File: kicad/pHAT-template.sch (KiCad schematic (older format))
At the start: 1 part

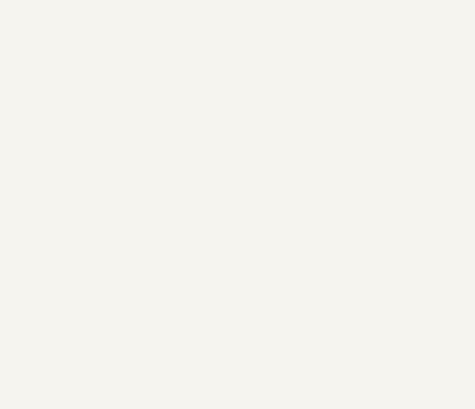
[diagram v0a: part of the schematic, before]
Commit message: added mounting holes and footprints
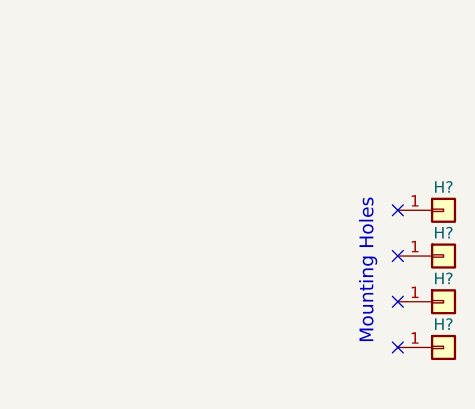
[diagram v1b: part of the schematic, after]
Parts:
- added H? (x4): Conn_01x01, Mounting_Holes:MountingHole_2.7mm_M2.5, symbol Conn_01x01
- J?: footprint (none) -> Pin_Headers:Pin_Header_Straight_2x20_Pitch2.54mm
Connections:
- no-connect marks 0 -> 4
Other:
- note added: "Mounting Holes"
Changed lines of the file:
@@
 F 0 "J?" H 2350 3100 50  0000 C CNN
 F 1 "Conn_02x20_Odd_Even" H 2350 1000 50  0001 C CNN
-F 2 "" H 2300 2100 50  0001 C CNN
+F 2 "Pin_Headers:Pin_Header_Straight_2x20_Pitch2.54mm" H 2300 2100 50  0001 C CNN
 F 3 "" H 2300 2100 50  0001 C CNN
 	1    2300 2100
@@
 Text Label 2100 3000 2    60   ~ 0
 BCM26
+$Comp
+L Conn_01x01 H?
+U 1 1 5A524F17
+P 6650 6900
+F 0 "H?" H 6650 7000 50  0000 C CNN
+F 1 "Conn_01x01" H 6650 6800 50  0001 C CNN
+F 2 "Mounting_Holes:MountingHole_2.7mm_M2.5" H 6650 6900 50  0001 C CNN
+F 3 "" H 6650 6900 50  0001 C CNN
+	1    6650 6900
+	1    0    0    -1
+$EndComp
+$Comp
+L Conn_01x01 H?
+U 1 1 5A525008
+P 6650 7100
+F 0 "H?" H 6650 7200 50  0000 C CNN
+F 1 "Conn_01x01" H 6650 7000 50  0001 C CNN
+F 2 "Mounting_Holes:MountingHole_2.7mm_M2.5" H 6650 7100 50  0001 C CNN
+F 3 "" H 6650 7100 50  0001 C CNN
+	1    6650 7100
+	1    0    0    -1
+$EndComp
+$Comp
+L Conn_01x01 H?
+U 1 1 5A525029
+P 6650 7300
+F 0 "H?" H 6650 7400 50  0000 C CNN
+F 1 "Conn_01x01" H 6650 7200 50  0001 C CNN
+F 2 "Mounting_Holes:MountingHole_2.7mm_M2.5" H 6650 7300 50  0001 C CNN
+F 3 "" H 6650 7300 50  0001 C CNN
+	1    6650 7300
+	1    0    0    -1
+$EndComp
+$Comp
+L Conn_01x01 H?
+U 1 1 5A525049
+P 6650 7500
+F 0 "H?" H 6650 7600 50  0000 C CNN
+F 1 "Conn_01x01" H 6650 7400 50  0001 C CNN
+F 2 "Mounting_Holes:MountingHole_2.7mm_M2.5" H 6650 7500 50  0001 C CNN
+F 3 "" H 6650 7500 50  0001 C CNN
+	1    6650 7500
+	1    0    0    -1
+$EndComp
+NoConn ~ 6450 6900
+NoConn ~ 6450 7100
+NoConn ~ 6450 7300
+NoConn ~ 6450 7500
+Text Notes 6350 6850 3    60   ~ 0
+Mounting Holes
 $EndSCHEMATC

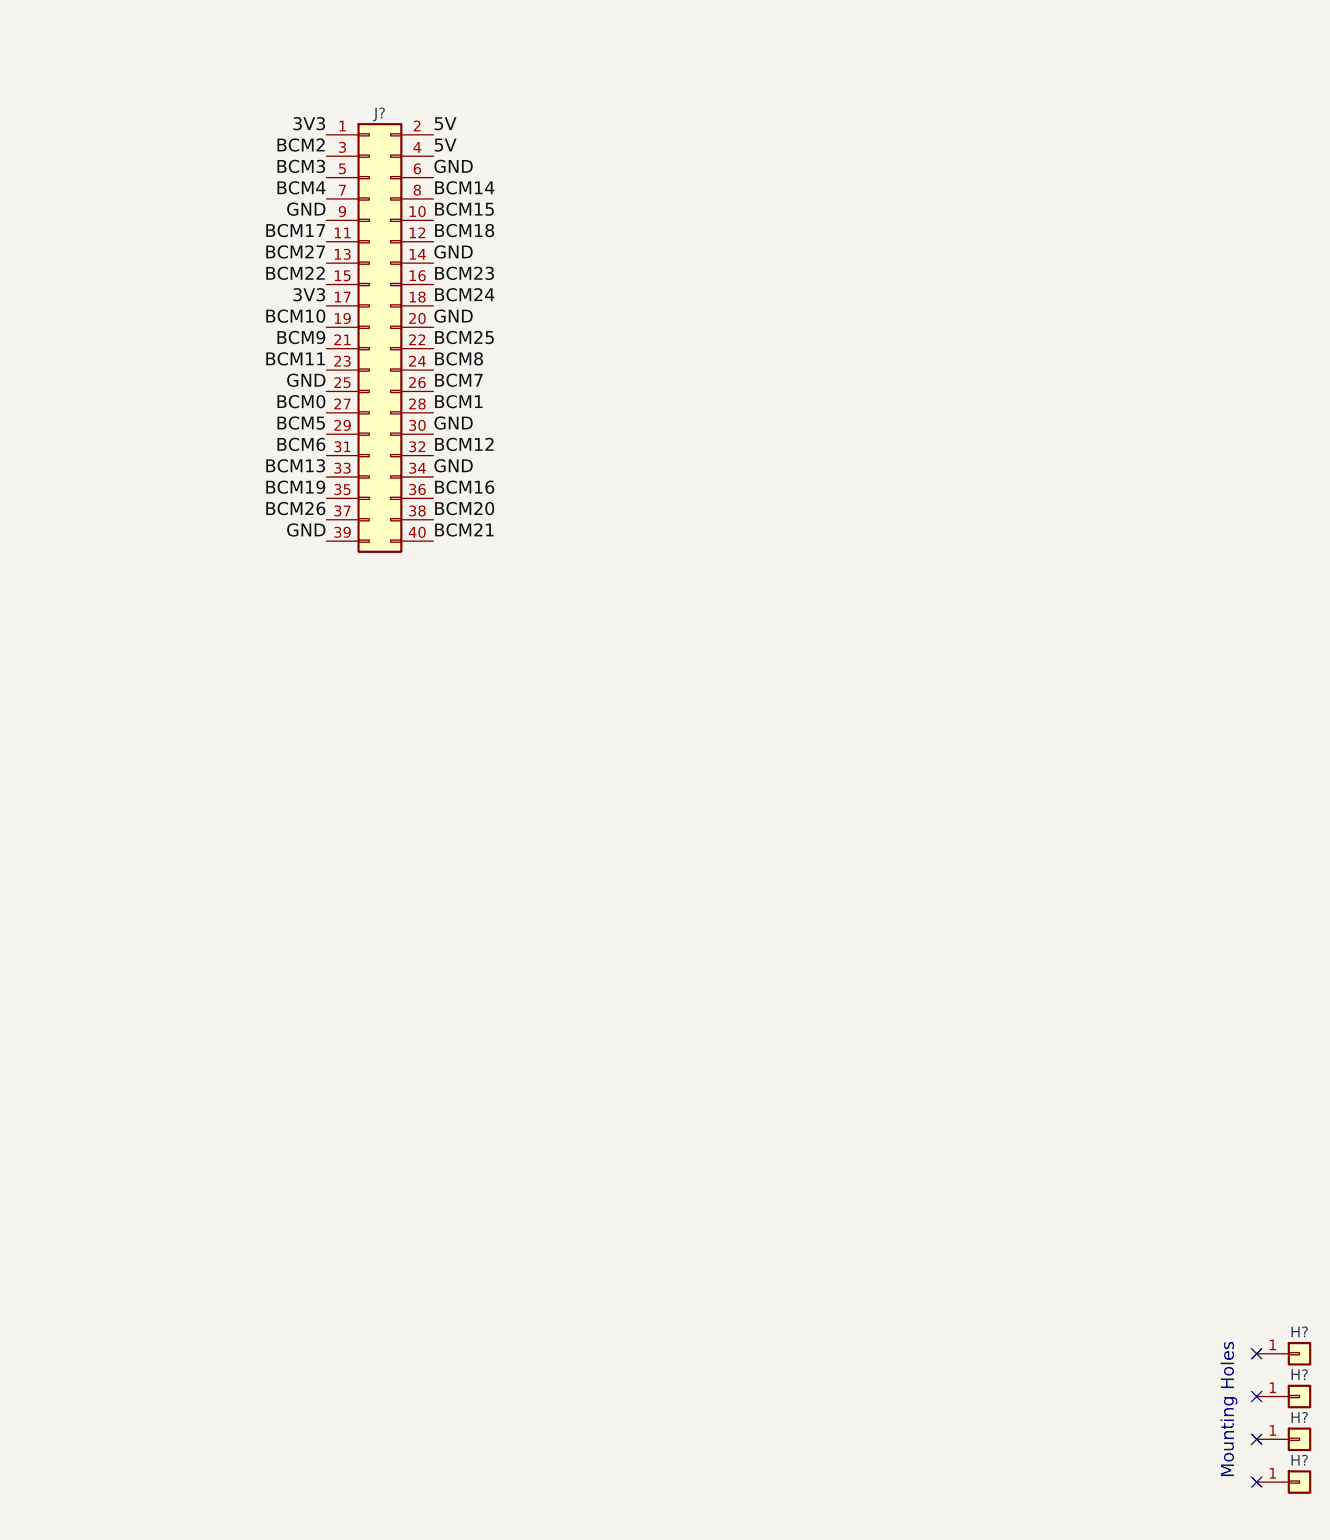
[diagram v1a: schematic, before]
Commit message: annotate schematic, generate netlist
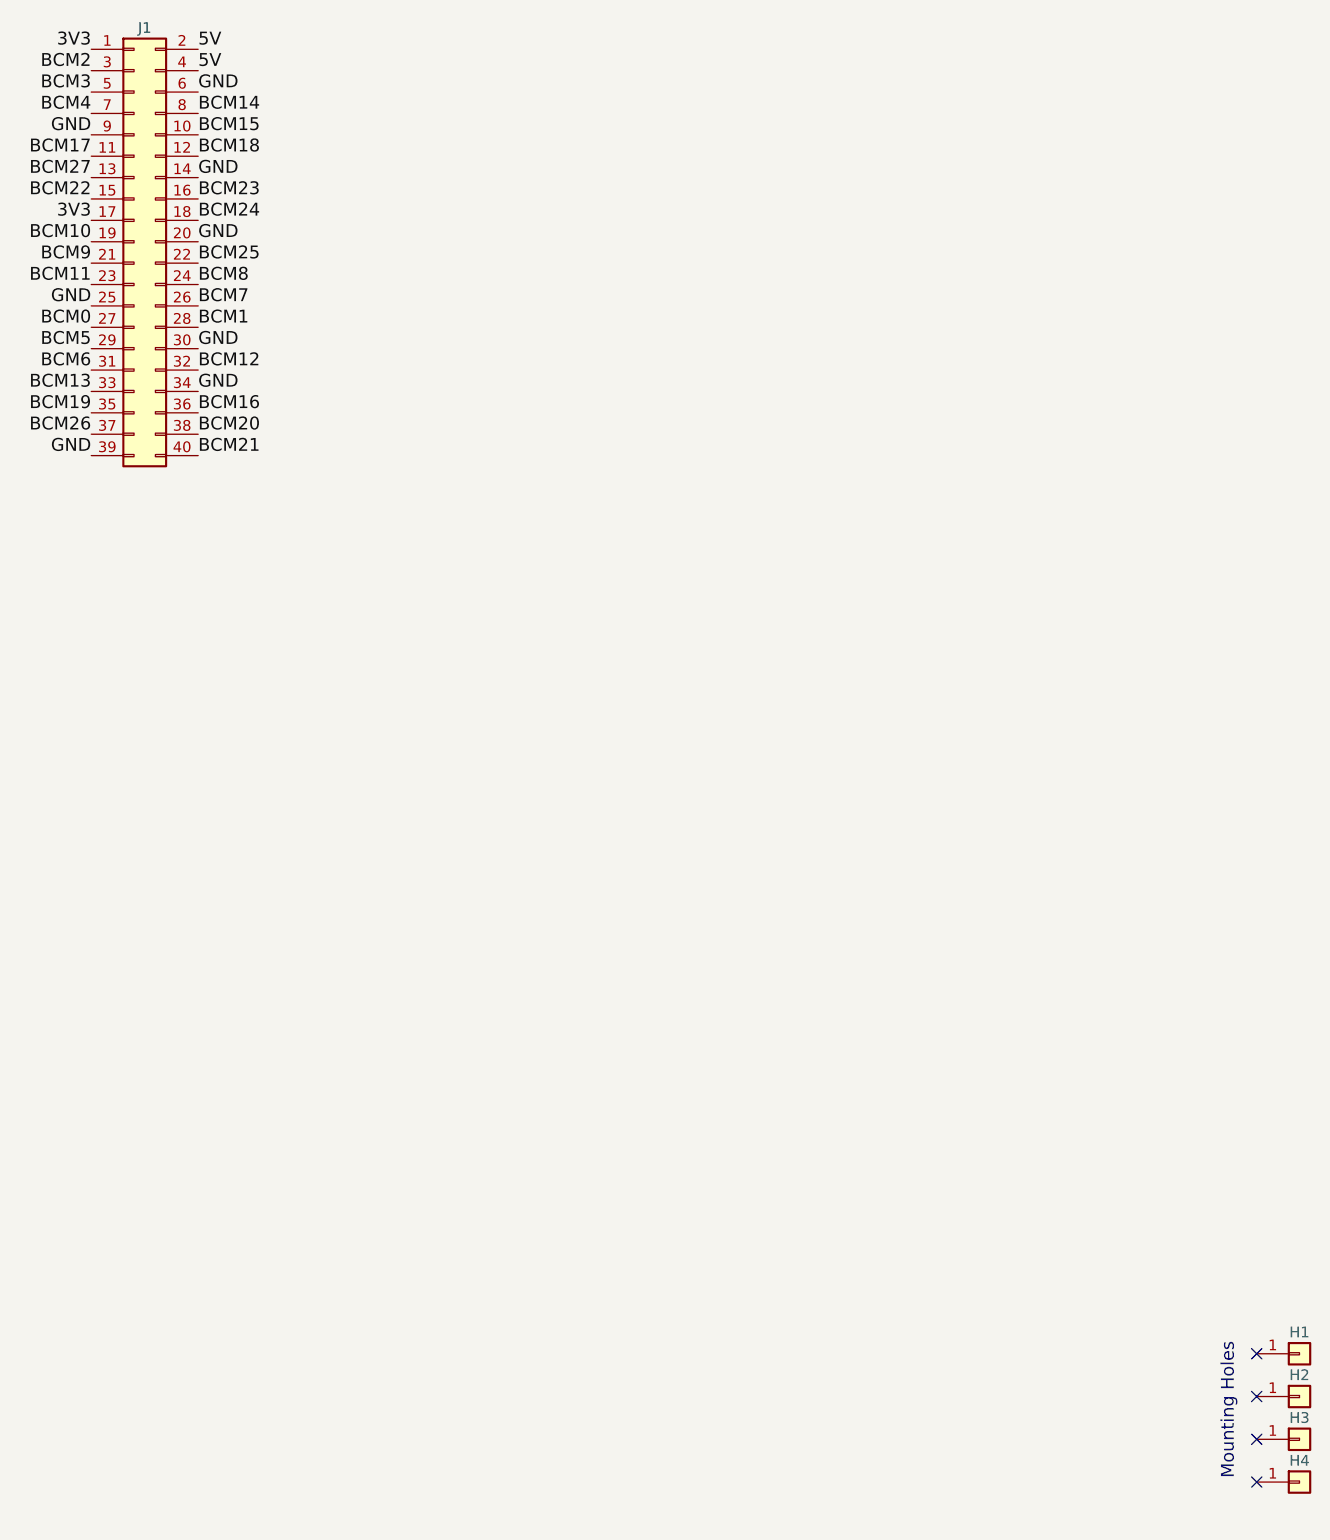
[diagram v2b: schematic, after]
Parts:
- gave numbers to parts that had none: 5
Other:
- moved on the sheet: J1
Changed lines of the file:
@@
 $EndDescr
 $Comp
-L Conn_02x20_Odd_Even J?
+L Conn_02x20_Odd_Even J1
 U 1 1 5A524BD5
-P 2300 2100
-F 0 "J?" H 2350 3100 50  0000 C CNN
-F 1 "Conn_02x20_Odd_Even" H 2350 1000 50  0001 C CNN
-F 2 "Pin_Headers:Pin_Header_Straight_2x20_Pitch2.54mm" H 2300 2100 50  0001 C CNN
-F 3 "" H 2300 2100 50  0001 C CNN
-	1    2300 2100
+P 1200 1700
+F 0 "J1" H 1250 2700 50  0000 C CNN
+F 1 "Conn_02x20_Odd_Even" H 1250 600 50  0001 C CNN
+F 2 "Pin_Headers:Pin_Header_Straight_2x20_Pitch2.54mm" H 1200 1700 50  0001 C CNN
+F 3 "" H 1200 1700 50  0001 C CNN
+	1    1200 1700
 	1    0    0    -1
 $EndComp
-Text Label 2600 1200 0    60   ~ 0
+Text Label 1500 800  0    60   ~ 0
 5V
-Text Label 2600 1300 0    60   ~ 0
+Text Label 1500 900  0    60   ~ 0
 5V
-Text Label 2600 1400 0    60   ~ 0
+Text Label 1500 1000 0    60   ~ 0
 GND
-Text Label 2600 1800 0    60   ~ 0
+Text Label 1500 1400 0    60   ~ 0
 GND
-Text Label 2600 2100 0    60   ~ 0
+Text Label 1500 1700 0    60   ~ 0
 GND
-Text Label 2600 2600 0    60   ~ 0
+Text Label 1500 2200 0    60   ~ 0
 GND
-Text Label 2600 2800 0    60   ~ 0
+Text Label 1500 2400 0    60   ~ 0
 GND
-Text Label 2100 3100 2    60   ~ 0
+Text Label 1000 2700 2    60   ~ 0
 GND
-Text Label 2100 2400 2    60   ~ 0
+Text Label 1000 2000 2    60   ~ 0
 GND
-Text Label 2100 1600 2    60   ~ 0
+Text Label 1000 1200 2    60   ~ 0
 GND
-Text Label 2100 1200 2    60   ~ 0
+Text Label 1000 800  2    60   ~ 0
 3V3
-Text Label 2100 2000 2    60   ~ 0
+Text Label 1000 1600 2    60   ~ 0
 3V3
-Text Label 2600 1500 0    60   ~ 0
+Text Label 1500 1100 0    60   ~ 0
 BCM14
-Text Label 2600 1600 0    60   ~ 0
+Text Label 1500 1200 0    60   ~ 0
 BCM15
-Text Label 2600 1700 0    60   ~ 0
+Text Label 1500 1300 0    60   ~ 0
 BCM18
-Text Label 2600 1900 0    60   ~ 0
+Text Label 1500 1500 0    60   ~ 0
 BCM23
-Text Label 2600 2000 0    60   ~ 0
+Text Label 1500 1600 0    60   ~ 0
 BCM24
-Text Label 2600 2200 0    60   ~ 0
+Text Label 1500 1800 0    60   ~ 0
 BCM25
-Text Label 2600 2300 0    60   ~ 0
+Text Label 1500 1900 0    60   ~ 0
 BCM8
-Text Label 2600 2400 0    60   ~ 0
+Text Label 1500 2000 0    60   ~ 0
 BCM7
-Text Label 2600 2500 0    60   ~ 0
+Text Label 1500 2100 0    60   ~ 0
 BCM1
-Text Label 2600 2700 0    60   ~ 0
+Text Label 1500 2300 0    60   ~ 0
 BCM12
-Text Label 2600 2900 0    60   ~ 0
+Text Label 1500 2500 0    60   ~ 0
 BCM16
-Text Label 2600 3000 0    60   ~ 0
+Text Label 1500 2600 0    60   ~ 0
 BCM20
-Text Label 2600 3100 0    60   ~ 0
+Text Label 1500 2700 0    60   ~ 0
 BCM21
-Text Label 2100 1300 2    60   ~ 0
+Text Label 1000 900  2    60   ~ 0
 BCM2
-Text Label 2100 1400 2    60   ~ 0
+Text Label 1000 1000 2    60   ~ 0
 BCM3
-Text Label 2100 1500 2    60   ~ 0
+Text Label 1000 1100 2    60   ~ 0
 BCM4
-Text Label 2100 1700 2    60   ~ 0
+Text Label 1000 1300 2    60   ~ 0
 BCM17
-Text Label 2100 1800 2    60   ~ 0
+Text Label 1000 1400 2    60   ~ 0
 BCM27
-Text Label 2100 1900 2    60   ~ 0
+Text Label 1000 1500 2    60   ~ 0
 BCM22
-Text Label 2100 2100 2    60   ~ 0
+Text Label 1000 1700 2    60   ~ 0
 BCM10
-Text Label 2100 2200 2    60   ~ 0
+Text Label 1000 1800 2    60   ~ 0
 BCM9
-Text Label 2100 2300 2    60   ~ 0
+Text Label 1000 1900 2    60   ~ 0
 BCM11
-Text Label 2100 2500 2    60   ~ 0
+Text Label 1000 2100 2    60   ~ 0
 BCM0
-Text Label 2100 2600 2    60   ~ 0
+Text Label 1000 2200 2    60   ~ 0
 BCM5
-Text Label 2100 2700 2    60   ~ 0
+Text Label 1000 2300 2    60   ~ 0
 BCM6
-Text Label 2100 2800 2    60   ~ 0
+Text Label 1000 2400 2    60   ~ 0
 BCM13
-Text Label 2100 2900 2    60   ~ 0
+Text Label 1000 2500 2    60   ~ 0
 BCM19
-Text Label 2100 3000 2    60   ~ 0
+Text Label 1000 2600 2    60   ~ 0
 BCM26
 $Comp
-L Conn_01x01 H?
+L Conn_01x01 H1
 U 1 1 5A524F17
 P 6650 6900
-F 0 "H?" H 6650 7000 50  0000 C CNN
+F 0 "H1" H 6650 7000 50  0000 C CNN
 F 1 "Conn_01x01" H 6650 6800 50  0001 C CNN
 F 2 "Mounting_Holes:MountingHole_2.7mm_M2.5" H 6650 6900 50  0001 C CNN
@@
 $EndComp
 $Comp
-L Conn_01x01 H?
+L Conn_01x01 H2
 U 1 1 5A525008
 P 6650 7100
-F 0 "H?" H 6650 7200 50  0000 C CNN
+F 0 "H2" H 6650 7200 50  0000 C CNN
 F 1 "Conn_01x01" H 6650 7000 50  0001 C CNN
 F 2 "Mounting_Holes:MountingHole_2.7mm_M2.5" H 6650 7100 50  0001 C CNN
@@
 $EndComp
 $Comp
-L Conn_01x01 H?
+L Conn_01x01 H3
 U 1 1 5A525029
 P 6650 7300
-F 0 "H?" H 6650 7400 50  0000 C CNN
+F 0 "H3" H 6650 7400 50  0000 C CNN
 F 1 "Conn_01x01" H 6650 7200 50  0001 C CNN
 F 2 "Mounting_Holes:MountingHole_2.7mm_M2.5" H 6650 7300 50  0001 C CNN
@@
 $EndComp
 $Comp
-L Conn_01x01 H?
+L Conn_01x01 H4
 U 1 1 5A525049
 P 6650 7500
-F 0 "H?" H 6650 7600 50  0000 C CNN
+F 0 "H4" H 6650 7600 50  0000 C CNN
 F 1 "Conn_01x01" H 6650 7400 50  0001 C CNN
 F 2 "Mounting_Holes:MountingHole_2.7mm_M2.5" H 6650 7500 50  0001 C CNN
